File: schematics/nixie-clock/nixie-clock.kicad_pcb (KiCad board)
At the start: 2 copper layers, 184.1 x 171.4 mm, 68 parts, among them J1 Barrel_Jack_Switch, J2 Conn_02x03_Odd_Even, J3 Conn_01x04, J4 Conn_01x07, J5 Conn_01x07, J6 Screw_Terminal_01x02, J7 Screw_Terminal_01x02, Q1 MJE13007, Q2 MJE13007, SW1 SW_Push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

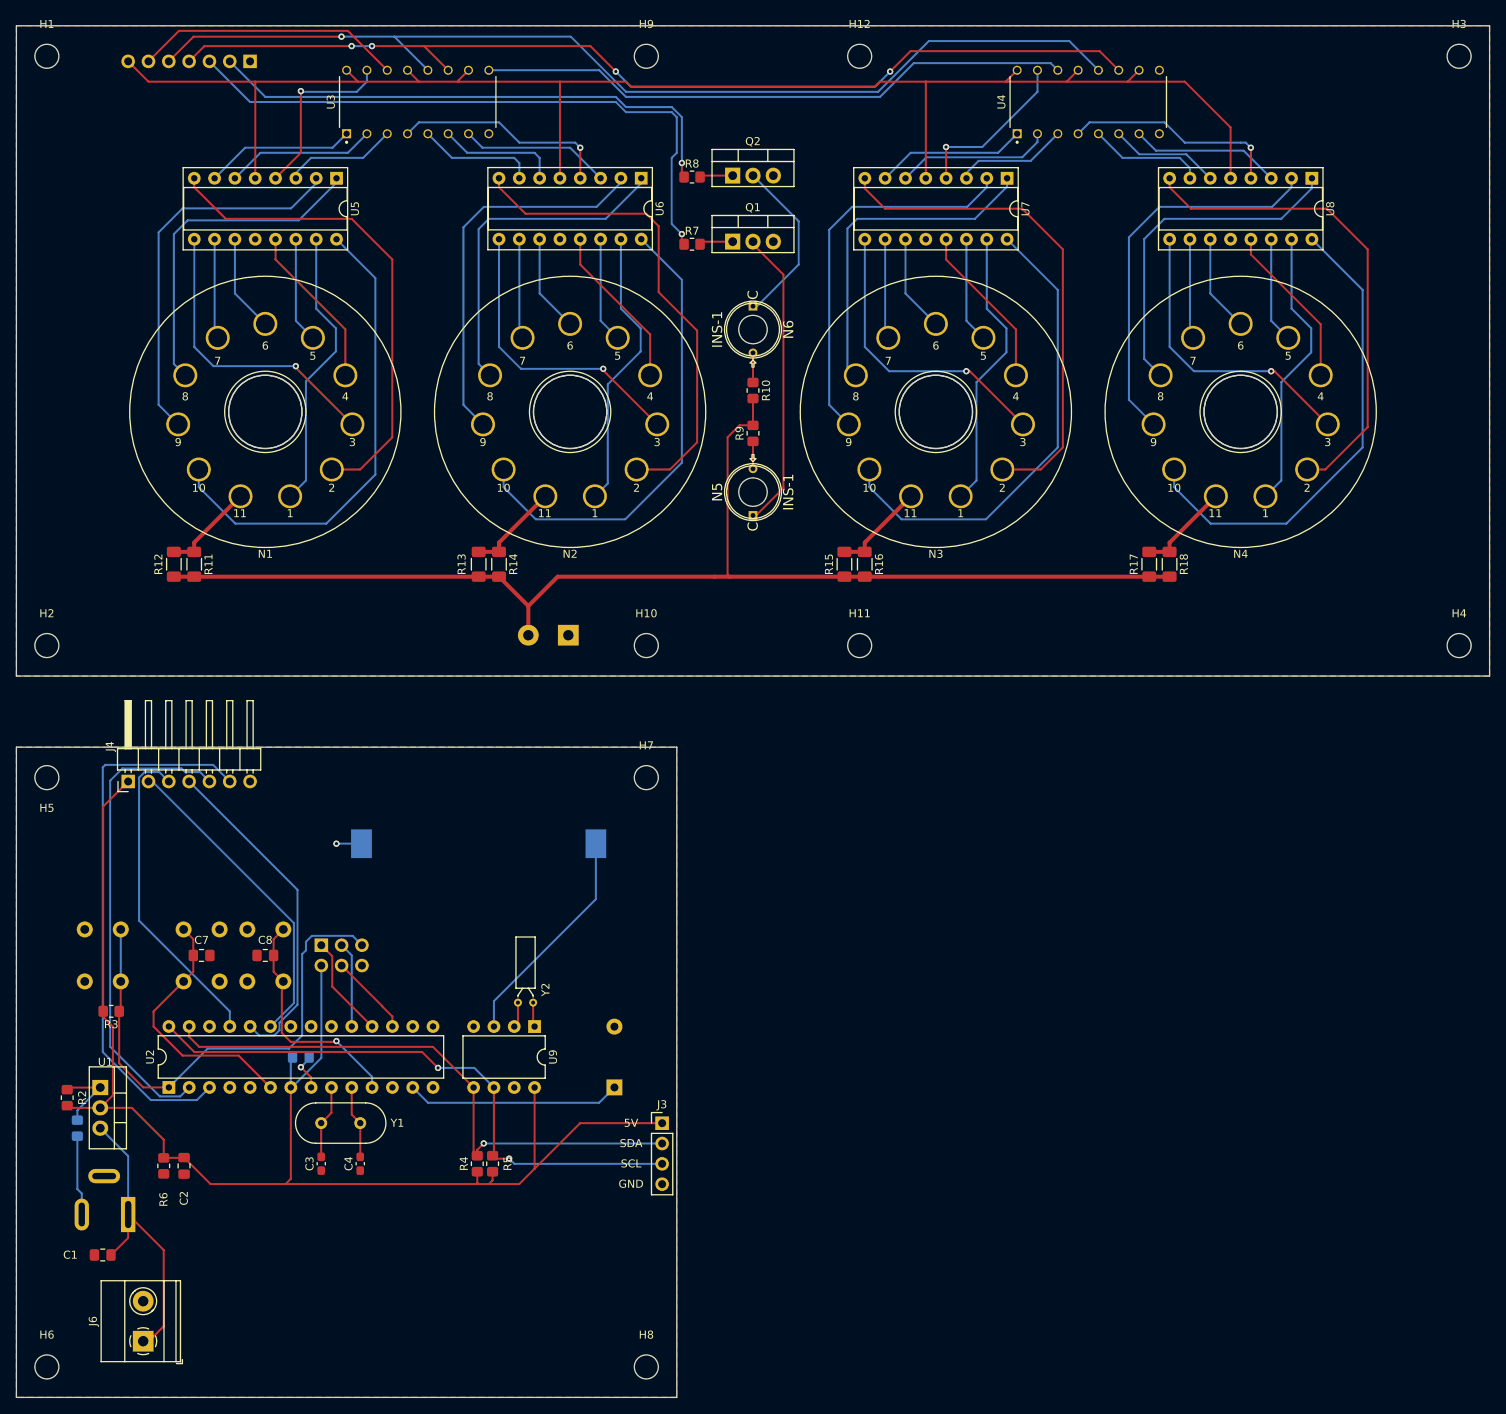
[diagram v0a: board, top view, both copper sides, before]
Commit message: pcb: pushed back angled goldpin headers, updated in-1 footprints on pcb
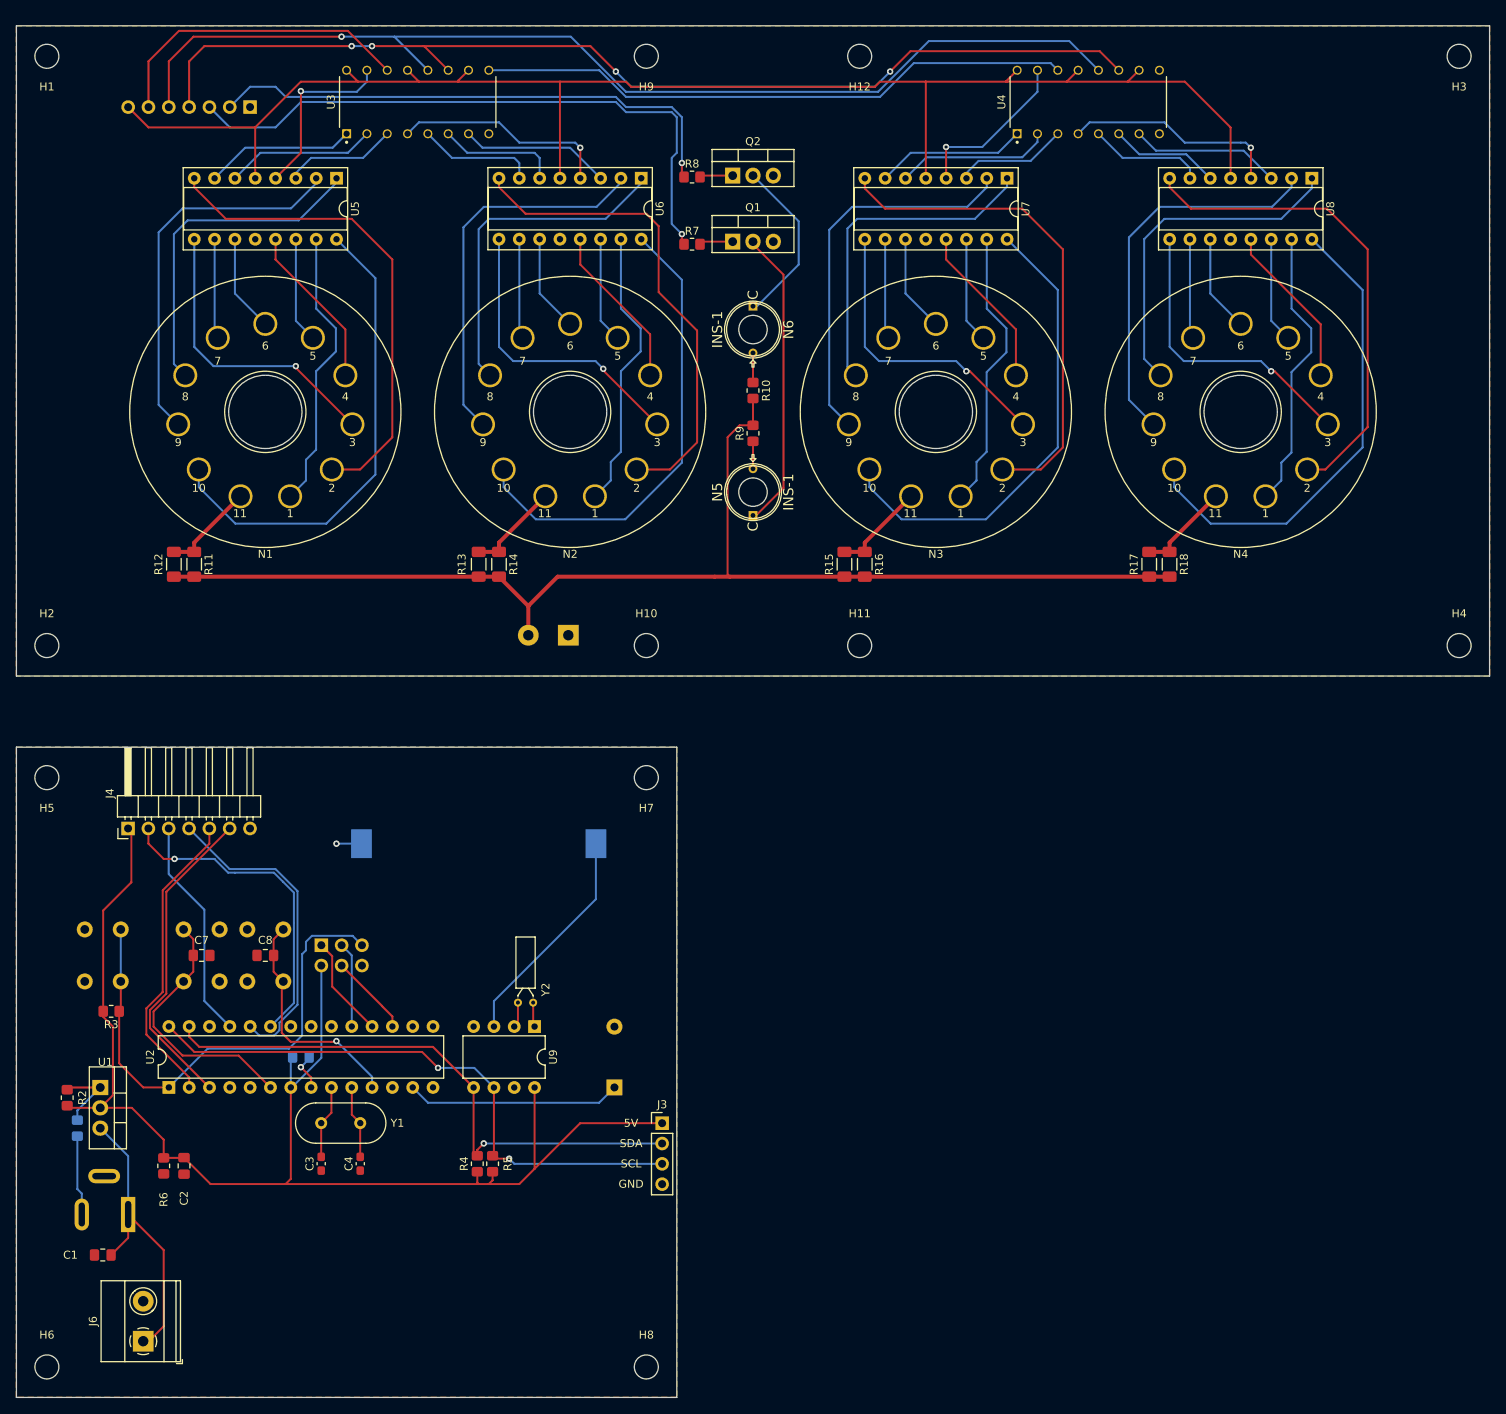
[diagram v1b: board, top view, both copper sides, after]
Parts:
- moved J4 5.88 mm to (70.5, 151.1)
- moved J5 5.72 mm to (85.7, 61.0)
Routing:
- net BULB2_CON: track 68.9 -> 39.6 mm
- net BULB1_CON: track 59.9 -> 37.9 mm
- net RCLK_CON: track 40.3 -> 27.9 mm
- net SRCLK: track 126.3 -> 132.1 mm
- net SER1: track 33.5 -> 39.2 mm
- net RCLK: track 130.4 -> 136.1 mm
- net +5V: track 172.8 -> 167.3 mm
- net +5VA: track 196.5 -> 193.2 mm
- net SRCLK_CON: track 42.0 -> 39.5 mm
- net SER1_CON: track 39.7 -> 40.6 mm, vias 0 -> 1

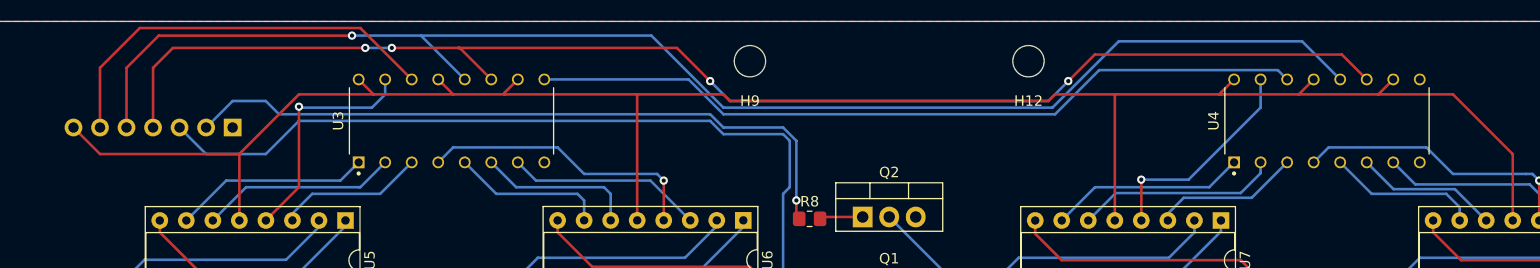
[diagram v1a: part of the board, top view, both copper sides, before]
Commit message: pcb: updated pcb according to the schematic, added silkscreen for headers
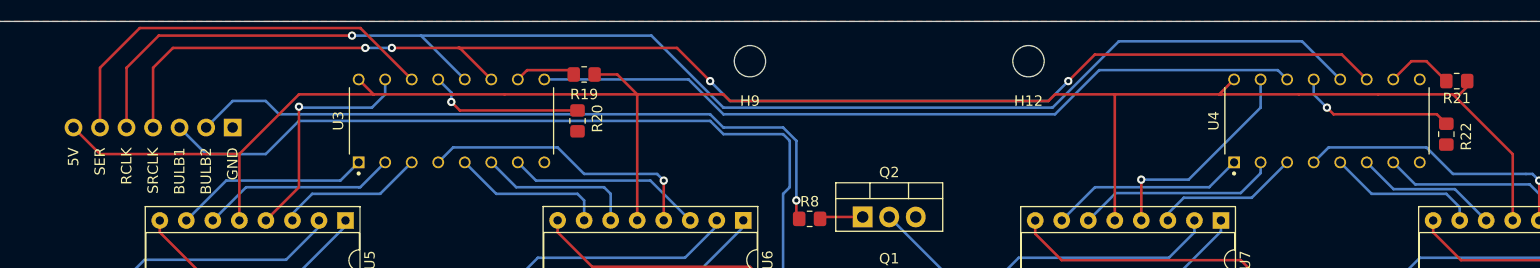
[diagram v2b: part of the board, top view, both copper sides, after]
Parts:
- added R19: 10k, Resistor_SMD:R_0805_2012Metric_Pad1.20x1.40mm_HandSolder, F.Cu at (119.4, 55.9)
- added R20: 10k, Resistor_SMD:R_0805_2012Metric_Pad1.20x1.40mm_HandSolder, F.Cu at (118.7, 60.3)
- added R21: 10k, Resistor_SMD:R_0805_2012Metric_Pad1.20x1.40mm_HandSolder, F.Cu at (202.9, 56.5)
- added R22: 10k, Resistor_SMD:R_0805_2012Metric_Pad1.20x1.40mm_HandSolder, F.Cu at (201.9, 61.6)
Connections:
- U3 pad 10: +5VA -> Net-(R19-Pad2)
- U3 pad 13: +5VA -> Net-(R20-Pad2)
- U4 pad 10: +5VA -> Net-(R21-Pad2)
- U4 pad 13: +5VA -> Net-(R22-Pad2)
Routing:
- net Net-(R22-Pad2): track 0.00 -> 15.3 mm, vias 0 -> 1
- net Net-(R20-Pad2): track 0.00 -> 15.1 mm, vias 0 -> 1
- net Net-(R21-Pad2): track 0.00 -> 6.59 mm
- net Net-(R19-Pad2): track 0.00 -> 5.89 mm
- net +5VA: track 193.2 -> 192.3 mm
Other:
- board text added: "BULB1"
- board text added: "BULB2"
- board text added: "RCLK"
- board text added: "SER"
- board text added: "SRCLK"
